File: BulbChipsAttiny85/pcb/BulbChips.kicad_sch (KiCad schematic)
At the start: 14 parts, among them J1 USB_C_Receptacle, SW1 SW_Push, U1 ATtiny85-20M, U2 BQ24040DSQR

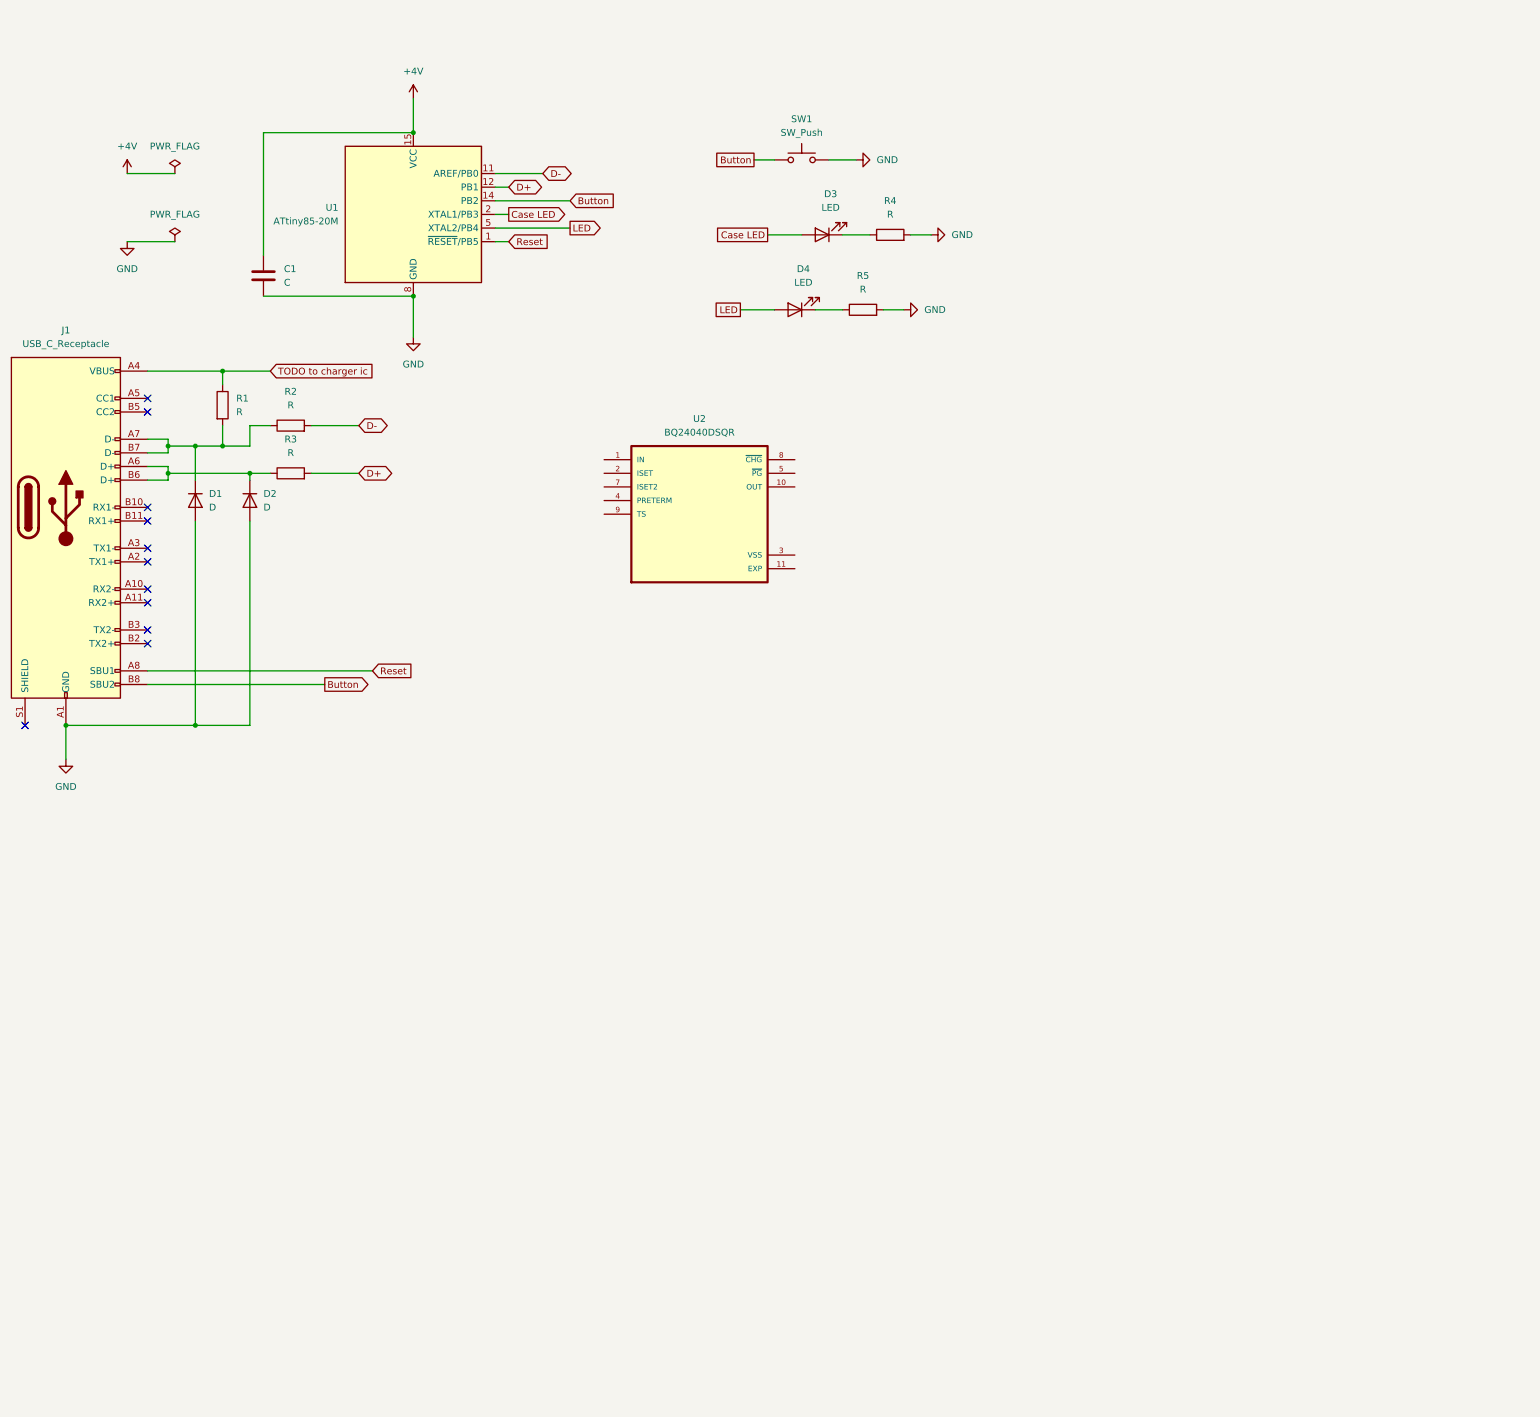
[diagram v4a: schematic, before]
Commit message: added more components to pcb
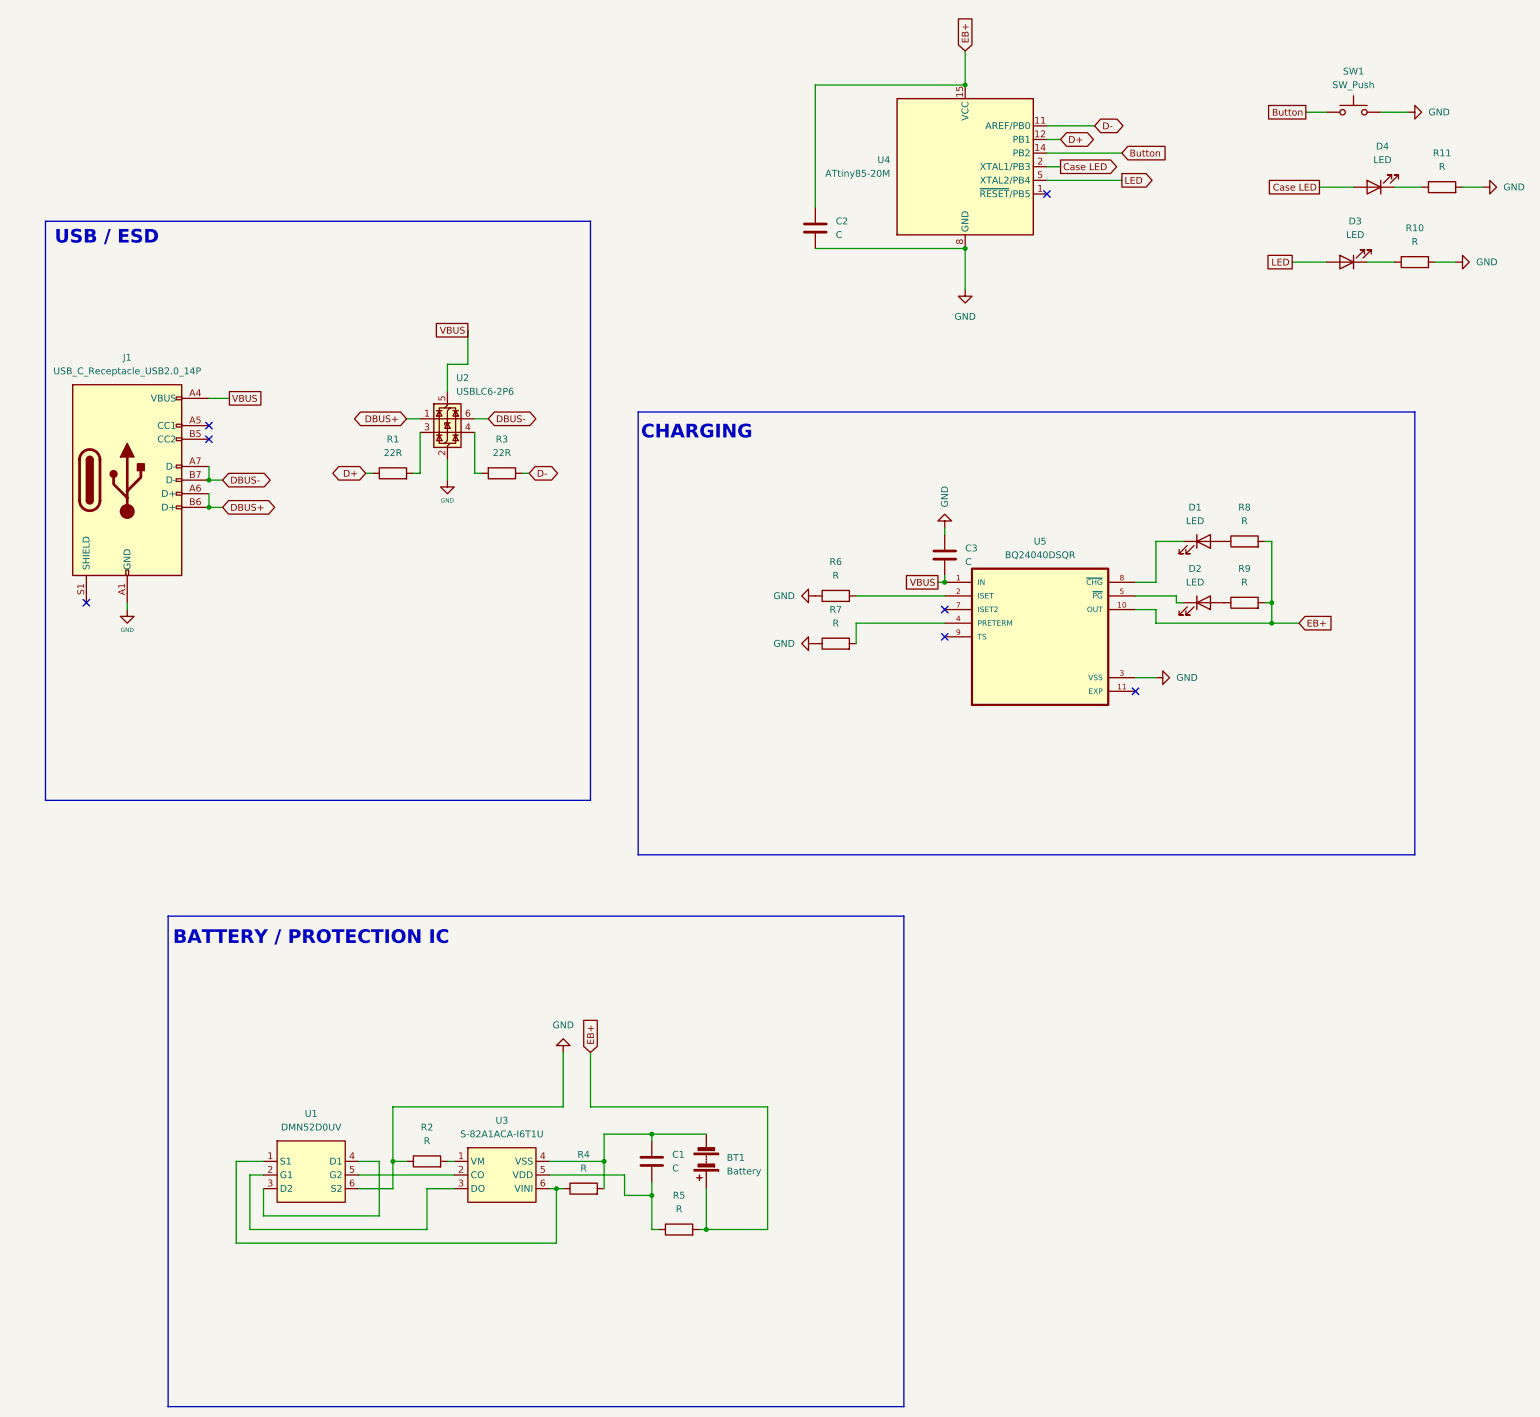
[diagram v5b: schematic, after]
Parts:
- removed D1, D2: D, symbol Device:D
- removed J1: USB_C_Receptacle, symbol Connector:USB_C_Receptacle
- removed U2: BQ24040DSQR, BQ24040DSQR:SON40P200X200X80-11N, symbol BQ24040DSQR:BQ24040DSQR
- added BT1: Battery, symbol Device:Battery
- added C1, C3: C, symbol Device:C
- added D1, D2: LED, symbol Device:LED
- added J1: USB_C_Receptacle_USB2.0_14P, symbol Connector:USB_C_Receptacle_USB2.0_14P
- added R4, R5, R6, R7, R8, R9: R, symbol Device:R
- added U1: DMN52D0UV, symbol BulbLib:DMN52D0UV
- added U2: USBLC6-2P6, Package_TO_SOT_SMD:SOT-666, symbol Power_Protection:USBLC6-2P6
- added U3: S-82A1ACA-I6T1U, symbol BulbLib:S-82A1ACA-I6T1U
- added U5: BQ24040DSQR, BQ24040DSQR:SON40P200X200X80-11N, symbol BQ24040DSQR:BQ24040DSQR
- R1, R3: value R -> 22R
- renumbered C1 to C2, D4 to D3, D3 to D4, R5 to R10, R4 to R11, U1 to U4
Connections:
- net TODO to charger ic is gone; now on net D+: R1.1
- net D+: no longer R3.2
- net D-: now also R3.1; no longer R2.2
- net GND: now also R2.1, C3.1, J1.A1 (GND), J1.A12 (GND), J1.B1 (GND), J1.B12 (GND), R6.1, R7.1, U1.6 (S2), U2.2 (GND), U5.3 (VSS)
- net at R1.2: now also U2.3 (I/O2); no longer R2.1
- net +4V renamed EB+
- net EB+: now also BT1.1 (+), R5.2, R8.2, R9.2, U5.10 (OUT)
- net Reset: no longer names the net of U4.1 (~{RESET}/PB5)
- new net: R6.2, U5.2 (ISET)
- new net: R7.2, U5.4 (PRETERM)
- new net: R2.2, U3.1 (VM)
- new net: D2.2 (A), R9.1
- new net: BT1.2 (-), C1.1, R4.2, U3.4 (VSS)
- new net: U1.5 (G2), U3.2 (CO)
- new net: U1.2 (G1), U3.3 (DO)
- new net: C1.2, R5.1, U3.5 (VDD)
- new net: R4.1, U1.1 (S1), U3.6 (VINI)
- new net: U1.3 (D2), U1.4 (D1)
- new net: D2.1 (K), U5.5 (~{PG})
- new net: D1.1 (K), U5.8 (~{CHG})
- new net: D1.2 (A), R8.1
- new net: R3.2, U2.4 (I/O2)
- new net DBUS+: J1.A6 (D+), J1.B6 (D+), U2.1 (I/O1)
- new net DBUS-: J1.A7 (D-), J1.B7 (D-), U2.6 (I/O1)
- new net VBUS: C3.2, J1.A4 (VBUS), J1.A9 (VBUS), J1.B4 (VBUS), J1.B9 (VBUS), U2.5 (VBUS), U5.1 (IN)
- no-connect marks 11 -> 7
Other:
- note added: "BATTERY / PROTECTION IC"
- note added: "CHARGING"
- note added: "USB / ESD"
- moved on the sheet: C2, D3, D4, R10, R11, SW1, U4

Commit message: fixed electrical rules checker errors, added some footprints, updated charger symbol
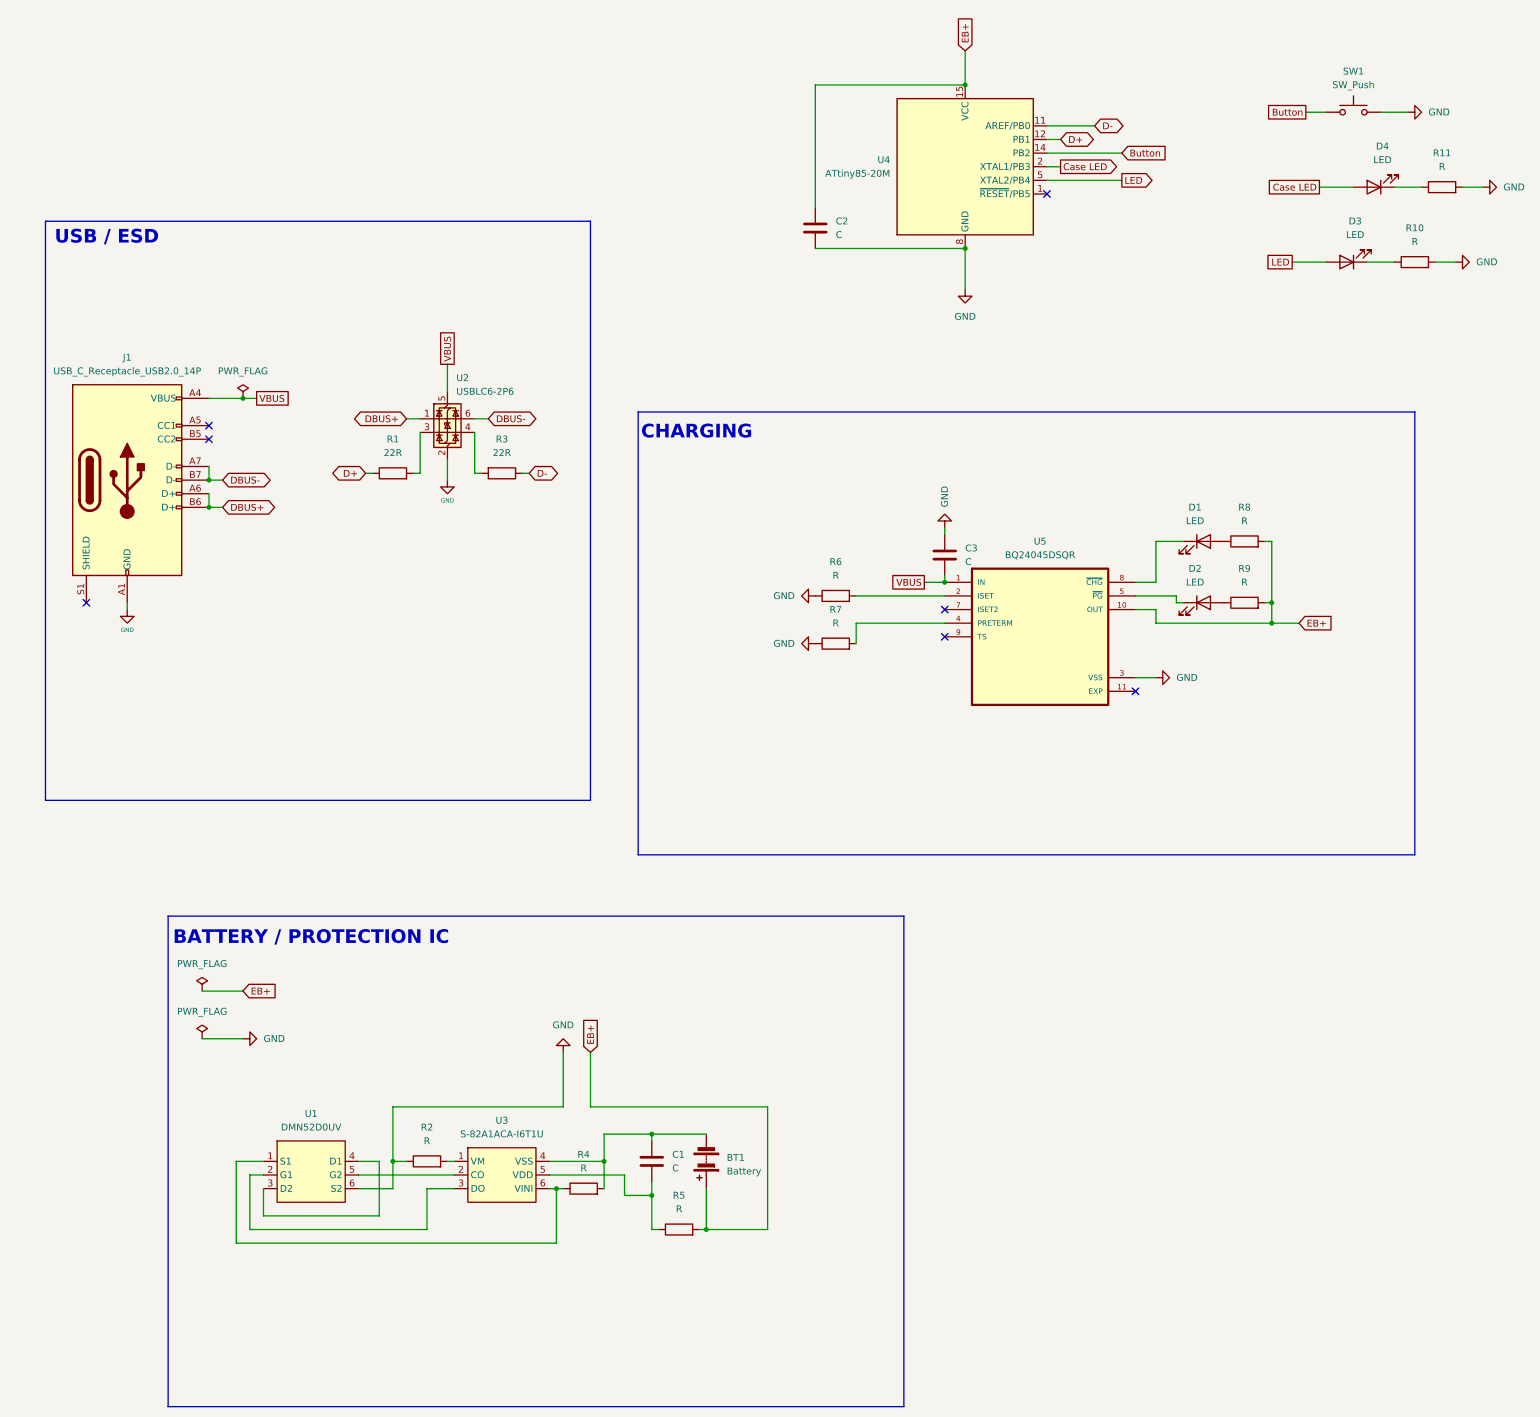
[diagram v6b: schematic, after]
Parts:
- removed U5: BQ24040DSQR, BQ24040DSQR:SON40P200X200X80-11N, symbol BQ24040DSQR:BQ24040DSQR
- added U5: BQ24045DSQR, Package_SON:WSON-10-1EP_2x3mm_P0.5mm_EP0.84x2.4mm_ThermalVias, symbol BulbLib:BQ24045DSQR
- U1: footprint (none) -> Package_TO_SOT_SMD:SOT-563
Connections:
- net EB+: now also U5.10 (OUT)
- net GND: now also U5.3 (VSS)
- net VBUS: now also U5.1 (IN)
- net at R6.2: now also U5.2 (ISET)
- net at R7.2: now also U5.4 (PRETERM)
- net at D2.1 (K): now also U5.5 (~{PG})
- net at D1.1 (K): now also U5.8 (~{CHG})

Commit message: added footprint for battery protection IC
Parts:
- U3: footprint (none) -> BulbLibrary:SNT-6A
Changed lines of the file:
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@@
 			)
 		)
-		(property "Footprint" ""
+		(property "Footprint" "BulbLibrary:SNT-6A"
 			(at 118.11 266.7 0)
 			(effects

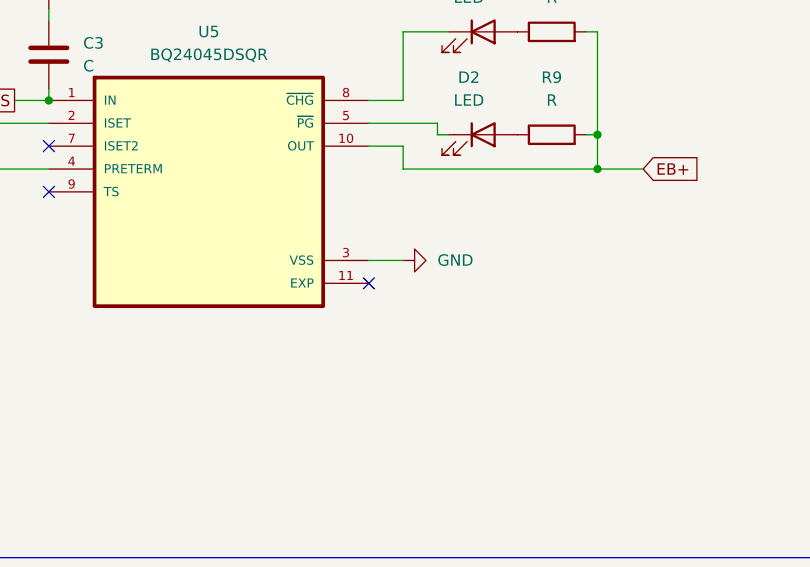
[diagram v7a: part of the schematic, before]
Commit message: Added better footprint for charger ic, and made sure thermal pad was connected to GND
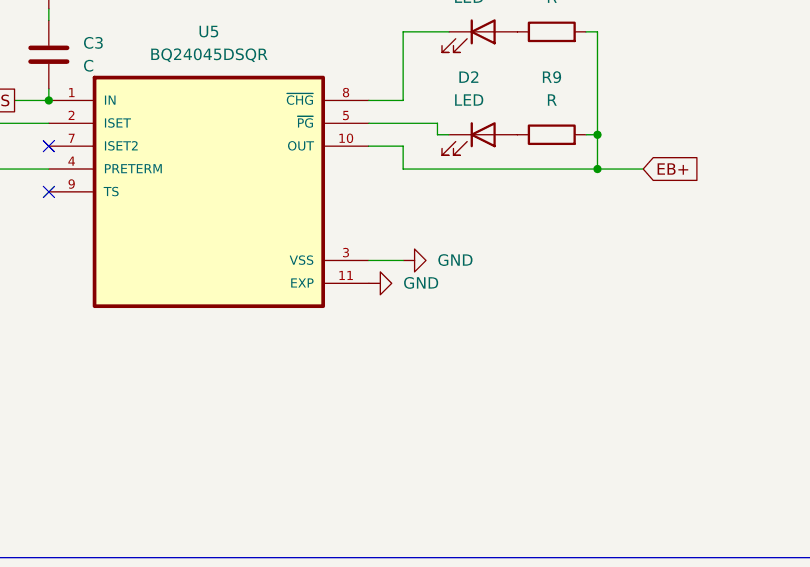
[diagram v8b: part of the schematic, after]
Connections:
- net GND: now also U5.11 (EXP)
- no-connect marks 7 -> 6
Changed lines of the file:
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@@
 	)
 	(no_connect
-		(at 236.22 173.99)
-	)
-	(no_connect
 		(at 63.5 127)
 	)
@@
 		(dnp no)
 		(fields_autoplaced yes)
-		(property "Reference" "#PWR010"
+		(property "Reference" "#PWR011"
 			(at 293.37 66.04 0)
 			(effects
@@
 			(project ""
 				(path "/fc2915fa-7a9c-445c-a5d7-b7fdeb691e1a"
-					(reference "#PWR010")
+					(reference "#PWR011")
 					(unit 1)
 				)
@@
 	)
 	(symbol
+		(lib_id "power:GND")
+		(at 236.22 173.99 90)
+		(unit 1)
+		(exclude_from_sim no)
+		(in_bom yes)
+		(on_board yes)
+		(dnp no)
+		(fields_autoplaced yes)
+		(property "Reference" "#PWR09"
+			(at 242.57 173.99 0)
+			(effects
+				(font
+					(size 1.27 1.27)
+				)
+				(hide yes)
+			)
+		)
+		(property "Value" "GND"
+			(at 240.03 173.9899 90)
+			(effects
+				(font
+					(size 1.27 1.27)
+				)
+				(justify right)
+			)
+		)
+		(property "Footprint" ""
+			(at 236.22 173.99 0)
+			(effects
+				(font
+					(size 1.27 1.27)
+				)
+				(hide yes)
+			)
+		)
+		(property "Datasheet" ""
+			(at 236.22 173.99 0)
+			(effects
+				(font
+					(size 1.27 1.27)
+				)
+				(hide yes)
+			)
+		)
+		(property "Description" "Power symbol creates a global label with name \"GND\" , ground"
+			(at 236.22 173.99 0)
+			(effects
+				(font
+					(size 1.27 1.27)
+				)
+				(hide yes)
+			)
+		)
+		(pin "1"
+		)
+		(instances
+			(project "BulbChips"
+				(path "/fc2915fa-7a9c-445c-a5d7-b7fdeb691e1a"
+					(reference "#PWR09")
+					(unit 1)
+				)
+			)
+		)
+	)
+	(symbol
 		(lib_id "Device:Battery")
 		(at 156.21 261.62 180)
@@
 		(dnp no)
 		(fields_autoplaced yes)
-		(property "Reference" "#PWR09"
+		(property "Reference" "#PWR010"
 			(at 246.38 171.45 0)
 			(effects
@@
 			(project ""
 				(path "/fc2915fa-7a9c-445c-a5d7-b7fdeb691e1a"
-					(reference "#PWR09")
+					(reference "#PWR010")
 					(unit 1)
 				)
@@
 		(dnp no)
 		(fields_autoplaced yes)
-		(property "Reference" "#PWR012"
+		(property "Reference" "#PWR013"
 			(at 307.34 80.01 0)
 			(effects
@@
 			(project "BulbChips"
 				(path "/fc2915fa-7a9c-445c-a5d7-b7fdeb691e1a"
-					(reference "#PWR012")
+					(reference "#PWR013")
 					(unit 1)
 				)
@@
 		(dnp no)
 		(fields_autoplaced yes)
-		(property "Reference" "#PWR011"
+		(property "Reference" "#PWR012"
 			(at 302.26 93.98 0)
 			(effects
@@
 			(project ""
 				(path "/fc2915fa-7a9c-445c-a5d7-b7fdeb691e1a"
-					(reference "#PWR011")
+					(reference "#PWR012")
 					(unit 1)
 				)
